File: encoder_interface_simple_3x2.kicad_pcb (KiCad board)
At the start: 2 copper layers, 69.8 x 40.6 mm, 13 parts, among them P1 BNC_DOUBLE_RA, P2 BNC_DOUBLE_RA, P3 HEADER_01X05_SMD_SHR, P4 HEADER_01X05_SMD_SHR, P5 HEADER_01X05_SMD_SHR, P6 HEADER_01X05_SMD_SHR, U1 SN74ABT541BDWR

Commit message: Finished version 1.0.
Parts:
- removed P4, P5, P6: HEADER_01X05_SMD_SHR, encoder_interface_simple_3x2:Header_Shrouded_5_Pin_SMD
- removed R3, R4: 180, encoder_interface_simple_3x2:SM1210
- R1, R2: value 180 -> 3.16k
- moved R2 19.1 mm to (109.9, 88.9), turned to 90 degrees
- moved P3 12.3 mm to (114.9, 88.9)
- moved R1 10.3 mm to (114.9, 88.9), turned to 90 degrees
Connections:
- MDB1 pad 3: /IN_0 -> /ENCODER_A_0
- MDB1 pad 4: /IN_1 -> /ENCODER_B_0
- MDB1 pad 5: /IN_2 -> (no net)
- MDB1 pad 6: /IN_3 -> (no net)
- P3 pad 1: Net-(P3-Pad1) -> GND
- P3 pad 2: GND -> (no net)
- P3 pad 3: VEE -> /ENCODER_A_0
- P3 pad 4: /IN_0 -> VEE
- P3 pad 5: GND -> /ENCODER_B_0
- R1 pad 1: Net-(P3-Pad1) -> VEE
- R1 pad 2: VEE -> /ENCODER_A_0
- R2 pad 1: Net-(P4-Pad1) -> VEE
- R2 pad 2: VEE -> /ENCODER_B_0
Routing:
- net GND: track 187.9 -> 121.0 mm
- net /OUT_3: track 112.1 -> 54.9 mm
- net /ENCODER_B_0: track 0.00 -> 48.3 mm
- net /IN_1: track 41.5 -> 0.00 mm
- net /IN_3: track 33.7 -> 0.00 mm
- net /IN_2: track 28.4 -> 0.00 mm
- net /ENCODER_A_0: track 0.00 -> 25.9 mm, vias 0 -> 1
- net /IN_0: track 13.4 -> 0.00 mm
- net VEE: track 102.2 -> 89.6 mm, vias 3 -> 1
- net /OUTPUT_2: track 9.37 -> 19.4 mm
- net /OUTPUT_0: track 33.7 -> 25.0 mm
- net Net-(P4-Pad1): track 7.27 -> 0.00 mm, vias 1 -> 0
- net /~ENABLE: track 43.6 -> 50.6 mm, vias 2 -> 1
- net /OUTPUT_3: track 15.3 -> 8.87 mm
- net Net-(P5-Pad1): track 4.90 -> 0.00 mm, vias 1 -> 0
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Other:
- board text added: "A_0"
- board text added: "B_0"
- board text added: "ENCODER"
- board text added: "Janelia Modular Device encoder_interface_simple part_number: 1231 03/2017 ver 1.0 3x2"
- board text added: "NC"
- board text added: "YEL"
- board text removed: "0"
- board text removed: "1"
- board text removed: "2"
- board text removed: "3"
- board text removed: "ANO"
- board text removed: "CAT"
- board text removed: "GRN"
- board text removed: "Janelia Modular Device encoder_interface_simple part_number: 1221 03/2017 ver 1.0 3x2"
- board text removed: "OUT"

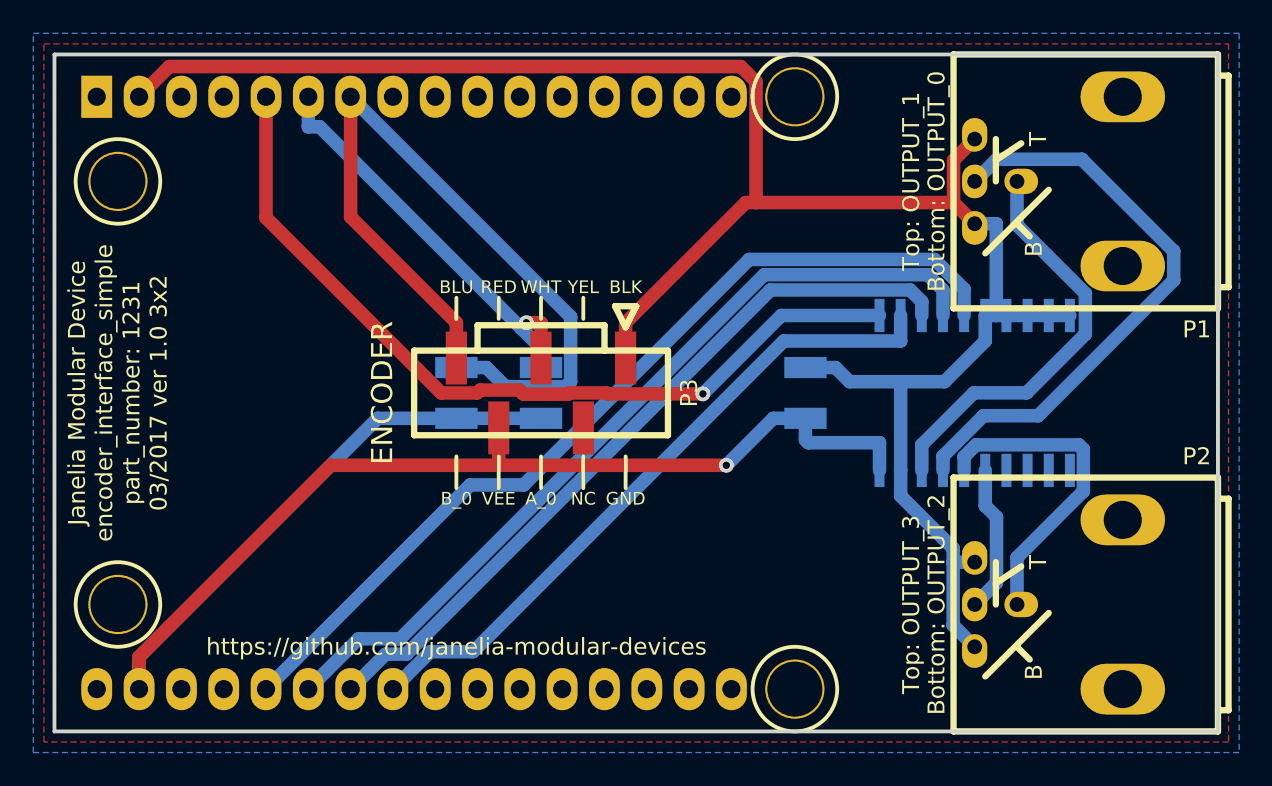
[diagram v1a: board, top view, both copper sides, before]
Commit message: Output buffered encoder signals only
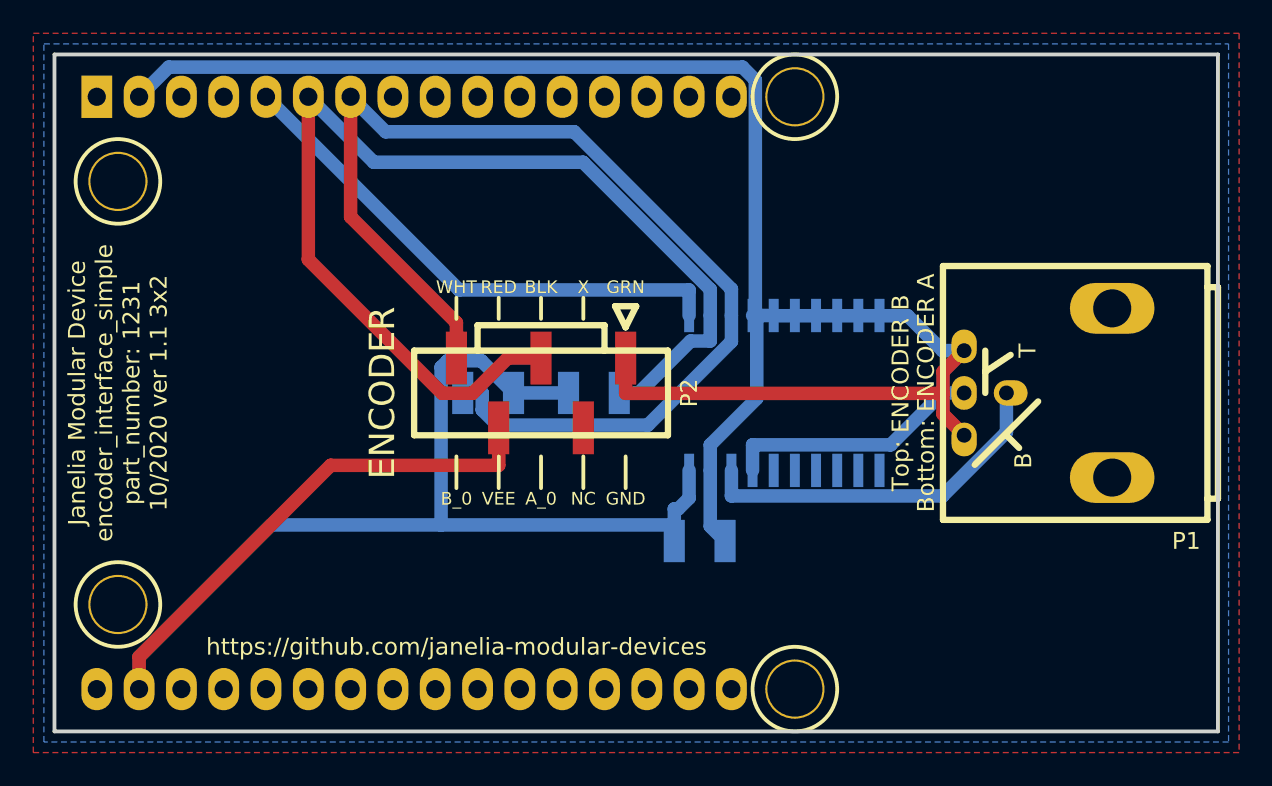
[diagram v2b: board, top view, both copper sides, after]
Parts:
- removed P3: HEADER_01X05_SMD_SHR, encoder_interface_simple_3x2:Header_Shrouded_5_Pin_SMD
- MDB1: value MODULAR_DEVICE_BASE_3X2_MALE -> VAL**
- P2: value BNC_DOUBLE_RA -> HEADER_01X05_SMD_SHR; footprint encoder_interface_simple_3x2:BNC_DOUBLE -> encoder_interface_simple_3x2:Header_Shrouded_5_Pin_SMD
- moved P2 37.2 mm to (114.9, 88.9), turned to 0 degrees
- moved P1 12.7 mm to (149.2, 88.9)
- moved U1 11.4 mm to (129.5, 88.9)
- moved C1 10.9 mm to (124.5, 97.8), turned to 270 degrees
- moved R1 3.17 mm to (118.1, 88.9), turned to 270 degrees
- moved R2 1.91 mm to (111.8, 88.9)
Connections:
- net /OUTPUT_0 renamed /ENCODER_A_BUF
- net /OUTPUT_1 renamed /ENCODER_B_BUF
- MDB1 pad 20: /OUT_0 -> (no net)
- MDB1 pad 21: /OUT_1 -> (no net)
- MDB1 pad 22: /OUT_2 -> (no net)
- MDB1 pad 23: /OUT_3 -> (no net)
- MDB1 pad 3: /ENCODER_A_0 -> /ENCODER_A
- MDB1 pad 4: /ENCODER_B_0 -> /ENCODER_B
- P2 pad 1: /OUTPUT_2 -> GND
- P2 pad 2: GND -> (no net)
- P2 pad 3: /OUTPUT_3 -> /ENCODER_A
- P2 pad 4: GND -> VEE
- R1 pad 2: /ENCODER_A_0 -> /ENCODER_A
- R2 pad 2: /ENCODER_B_0 -> /ENCODER_B
- U1 pad 15: /OUTPUT_3 -> (no net)
- U1 pad 16: /OUTPUT_2 -> (no net)
- U1 pad 2: /OUT_0 -> /ENCODER_A
- U1 pad 3: /OUT_1 -> /ENCODER_B
- U1 pad 4: /OUT_2 -> GND
- U1 pad 5: /OUT_3 -> GND
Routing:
- net /ENCODER_B: track 0.00 -> 68.7 mm
- net /ENCODER_A: track 0.00 -> 66.7 mm
- net /OUT_3: track 54.9 -> 0.00 mm
- net /OUT_2: track 50.3 -> 0.00 mm
- net /ENCODER_B_0: track 48.3 -> 0.00 mm
- net /OUT_1: track 45.3 -> 0.00 mm
- net /OUT_0: track 40.7 -> 0.00 mm
- net /ENCODER_A_0: track 25.9 -> 0.00 mm, vias 1 -> 0
- net /ENCODER_B_BUF: track 35.6 -> 15.5 mm
- net /OUTPUT_2: track 19.4 -> 0.00 mm
- net /~ENABLE: track 50.6 -> 31.7 mm, vias 1 -> 0
- net GND: track 121.0 -> 108.2 mm
- net /OUTPUT_3: track 8.87 -> 0.00 mm
- net /ENCODER_A_BUF: track 25.0 -> 22.0 mm
- net VEE: track 89.6 -> 90.7 mm, vias 1 -> 0
- added copper zone on B.Cu, net VEE
- removed copper zone on B.Cu, net GND
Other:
- board text added: "GRN"
- board text added: "Janelia Modular Device encoder_interface_simple part_number: 1231 10/2020 ver 1.1 3x2"
- board text added: "X"
- board text removed: "BLU"
- board text removed: "Janelia Modular Device encoder_interface_simple part_number: 1231 03/2017 ver 1.0 3x2"
- board text removed: "YEL"
